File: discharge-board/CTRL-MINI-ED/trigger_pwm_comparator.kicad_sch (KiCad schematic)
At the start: 3 parts, among them U8 BD33FC0FP

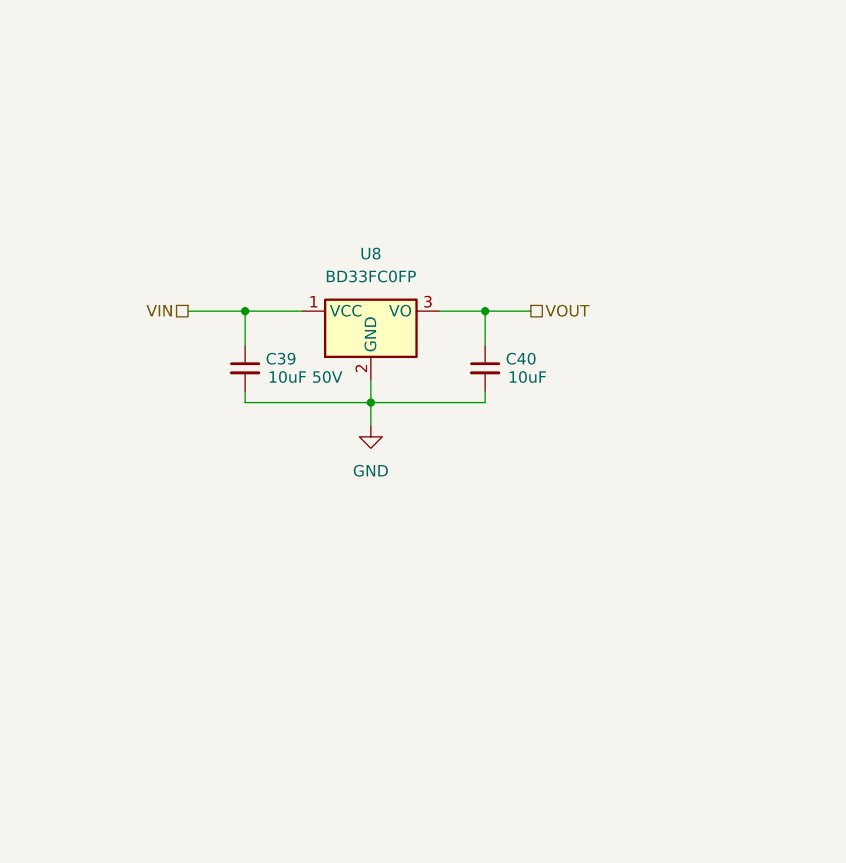
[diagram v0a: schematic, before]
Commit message: Add PWM voltage divider and refactor
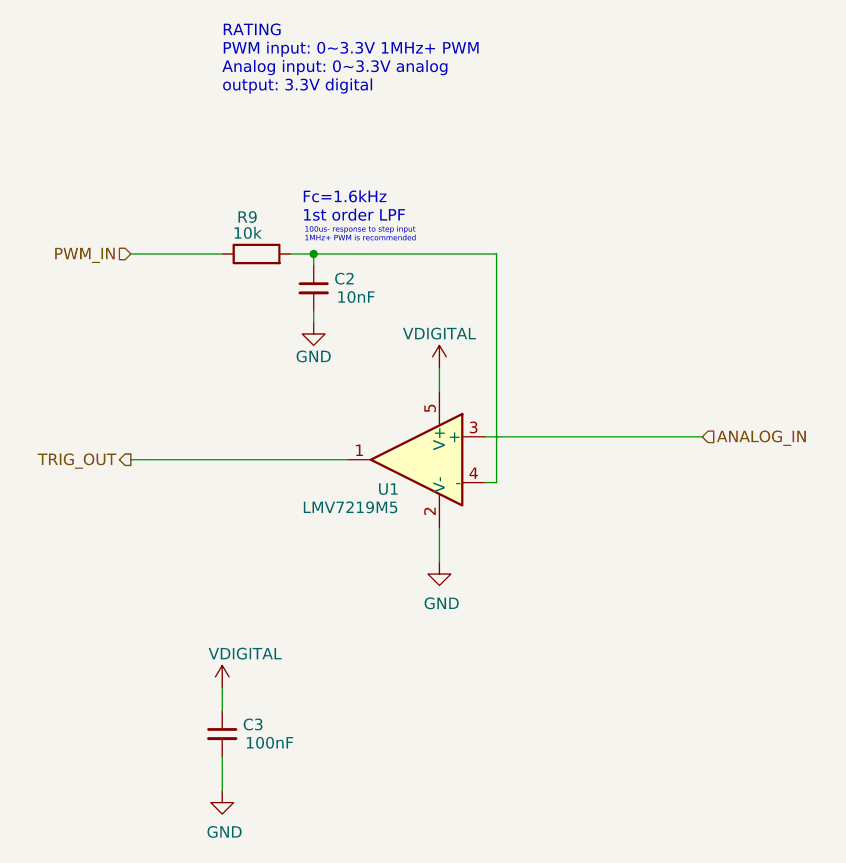
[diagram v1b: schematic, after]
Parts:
- removed C39: 10uF 50V, Capacitor_SMD:C_1206_3216Metric, symbol Device:C_Small
- removed C40: 10uF, Capacitor_SMD:C_0603_1608Metric, symbol Device:C_Small
- removed U8: BD33FC0FP, Package_TO_SOT_SMD:TO-252-2, symbol Regulator_Linear:BD33FC0FP
- added C2: 10nF, Capacitor_SMD:C_0603_1608Metric, symbol Device:C_Small
- added C3: 100nF, Capacitor_SMD:C_0603_1608Metric, symbol Device:C_Small
- added R9: 10k, Resistor_SMD:R_0603_1608Metric, symbol Device:R
- added U1: LMV7219M5, Package_TO_SOT_SMD:SOT-23-5, symbol Comparator:LMV7219M5
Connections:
- net GND: now also C2.2, C3.2, U1.2 (V-)
- new net: C2.1, R9.2, U1.4 (-)
- new net ANALOG_IN: U1.3 (+)
- new net PWM_IN: R9.1
- new net TRIG_OUT: U1.1
- new net VDIGITAL: C3.1, U1.5 (V+)
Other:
- note added: "100us- response to step input 1MHz+ PWM is recommended"
- note added: "Fc=1.6kHz 1st order LPF"
- note added: "RATING PWM input: 0~3.3V 1MHz+ PWM Analog input: 0~3.3V analog output: 3.3V digital"
